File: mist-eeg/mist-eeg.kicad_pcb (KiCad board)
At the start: 4 copper layers, 50 x 75 mm, 234 parts, among them J1 Power_5V-14V, J10 J1310, J3 Audio, J4 Electrodes, J5 Micro_SD_Card_Det, J6 Extra GPIOs, J7 Digital buses, J8 J1312, J9 J1311, Q1 NMOS_DGS (3V3), Q3 NMOS_DGS (3.3V), Q4 PMOS_DGS (3.3V @ 1A), SW1 START, SW2 USER, SW3 SD_RST, SW4 RESET, SW5 ONOFF, U1 LTC2947, U10 ADAU1372, U11 ADS1299, U12 NX5427001Z, U5 TPS63070, U6 LT3042xMSE, U7 LT3042xMSE, U8 TPS63070, U9 TPS63070

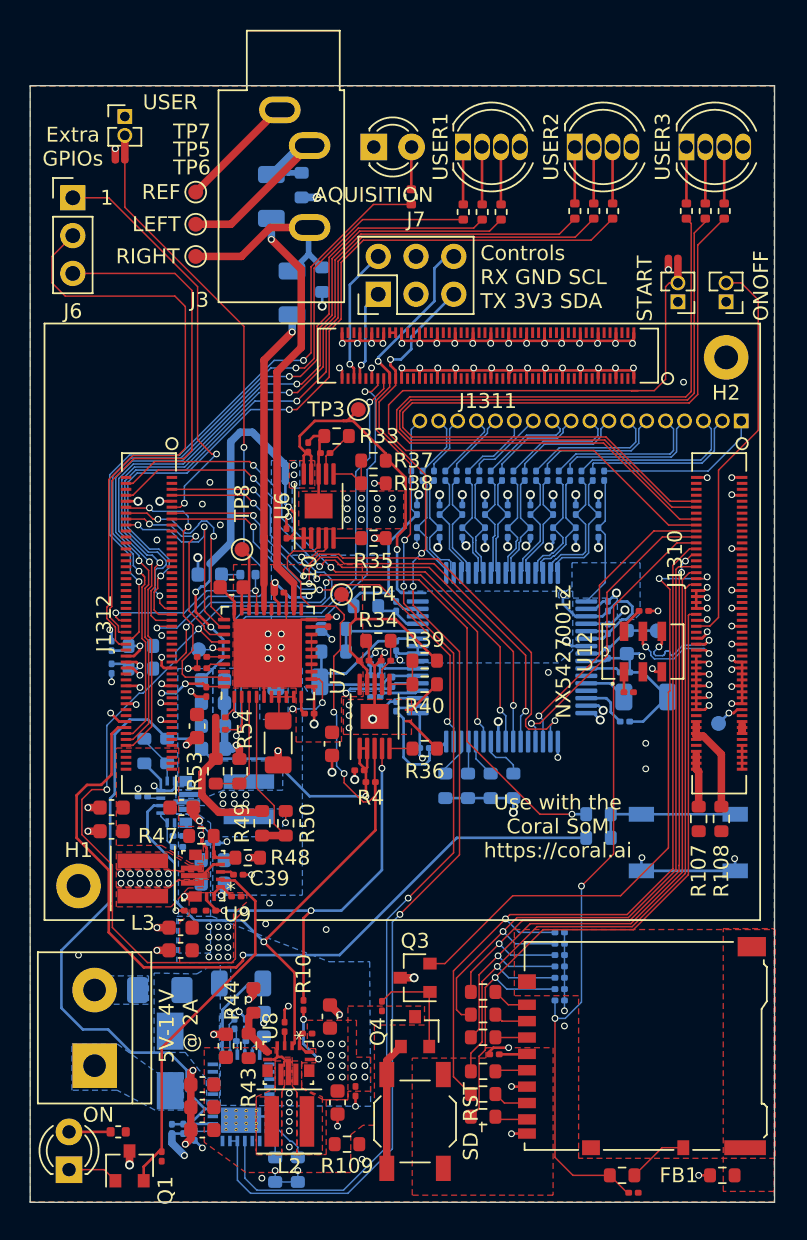
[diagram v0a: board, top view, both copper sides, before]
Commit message: Update footprints based upon piece availability & generate manufacturing files
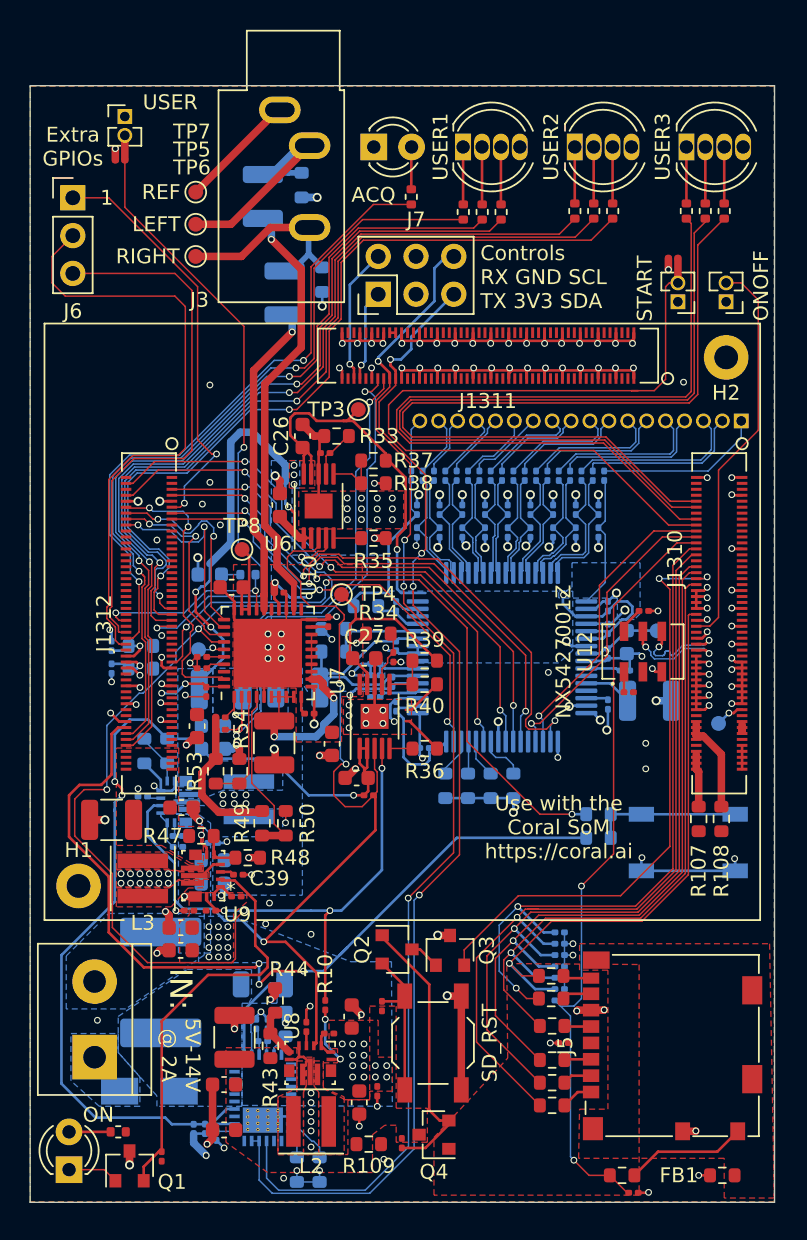
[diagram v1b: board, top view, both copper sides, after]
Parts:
- removed C21, C35, C42: 22uF, Capacitor_SMD:C_0603_1608Metric
- added Q2: NMOS_DGS (3.3V), Package_TO_SOT_SMD:SOT-23, F.Cu at (223.6, 92.0)
- added R11: 4k7, Resistor_SMD:R_0201_0603Metric, F.Cu at (222.6, 95.8)
- C19: value 22uF -> 10uF
- C20, C34, C41: value 22uF -> 47uF; footprint Capacitor_SMD:C_0603_1608Metric -> Capacitor_SMD:C_1210_3225Metric
- C22, C23, C26, C27: value 4u7F -> 10uF; footprint Capacitor_SMD:C_0201_0603Metric -> Capacitor_SMD:C_0603_1608Metric
- C44, C45, C50, C58, C65: footprint Capacitor_SMD:C_1206_3216Metric -> Capacitor_SMD:C_1210_3225Metric
- D5: value AQUISITION -> ACQ
- F1: footprint Fuse:Fuse_1206_3216Metric_Pad1.42x1.75mm_HandSolder -> Fuse:Fuse_2920_7451Metric
- J5: footprint Connector_Card:microSD_HC_Hirose_DM3AT-SF-PEJM5 -> Connector_Card:microSD_HC_Molex_104031-0811
- R47: value 52k5 -> 52k3
- moved R104 10.5 mm to (234.0, 93.8)
- moved R106 9.30 mm to (224.0, 105.0), turned to 270 degrees
- moved R99 8.92 mm to (234.1, 102.5)
- moved R103 7.88 mm to (234.0, 95.3)
- moved Q4 7.04 mm to (226.1, 104.5), turned to 180 degrees
- moved R100 6.51 mm to (234.1, 101.0)
- moved R102 5.55 mm to (234.1, 97.2)
- moved SW3 5.41 mm to (226.1, 98.3), turned to 270 degrees
- moved R101 4.88 mm to (234.1, 99.4)
- moved C87 4.70 mm to (234.8, 98.3)
- moved Q3 2.99 mm to (227.2, 92.1), turned to 90 degrees
- moved D1 2.47 mm to (207.0, 101.5), turned to 180 degrees
- moved J5 2.03 mm to (242.1, 98.5)
- moved C22 1.96 mm to (215.8, 62.2)
- moved C64 1.62 mm to (237.8, 75.6), turned to 90 degrees
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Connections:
- Q3 pad 1: Net-(Q3-Pad1) -> Net-(Q2-Pad3)
- Q4 pad 1: Net-(Q4-Pad1) -> /SD_DATA/+PWR
- Q4 pad 2: Net-(Q3-Pad1) -> Net-(Q2-Pad1)
- R106 pad 2: Net-(Q3-Pad1) -> Net-(Q2-Pad1)
- SW3 pad 1: Net-(Q4-Pad1) -> GND
- SW3 pad 2: /SD_DATA/+PWR -> Net-(Q2-Pad2)
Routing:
- net Net-(Q2-Pad1): track 0.00 -> 18.7 mm
- net Net-(Q2-Pad2): track 0.00 -> 10.8 mm
- net /SD_CLK: track 48.2 -> 38.6 mm
- net /SD_DAT0: track 44.1 -> 53.4 mm, vias 3 -> 1
- net Net-(Q4-Pad1): track 8.58 -> 0.00 mm
- net Net-(Q3-Pad1): track 7.18 -> 0.00 mm
- net /SD_CMD: track 52.4 -> 45.4 mm, vias 1 -> 2
- net Net-(J5-Pad10): track 4.05 -> 8.17 mm
- net /audio/CM: track 11.8 -> 15.4 mm
- net /SD_DAT3: track 47.2 -> 43.7 mm
- net /SD_DAT1: track 46.4 -> 49.9 mm
- net /SoM/~PWR_ON~: track 53.8 -> 56.9 mm, vias 1 -> 3
- net /+5V0_ANA: track 53.9 -> 56.8 mm
- net /power/+5V25: track 93.6 -> 96.4 mm, vias 4 -> 6
- net /power/PG: track 25.0 -> 27.7 mm
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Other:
- board text added: "IN:"

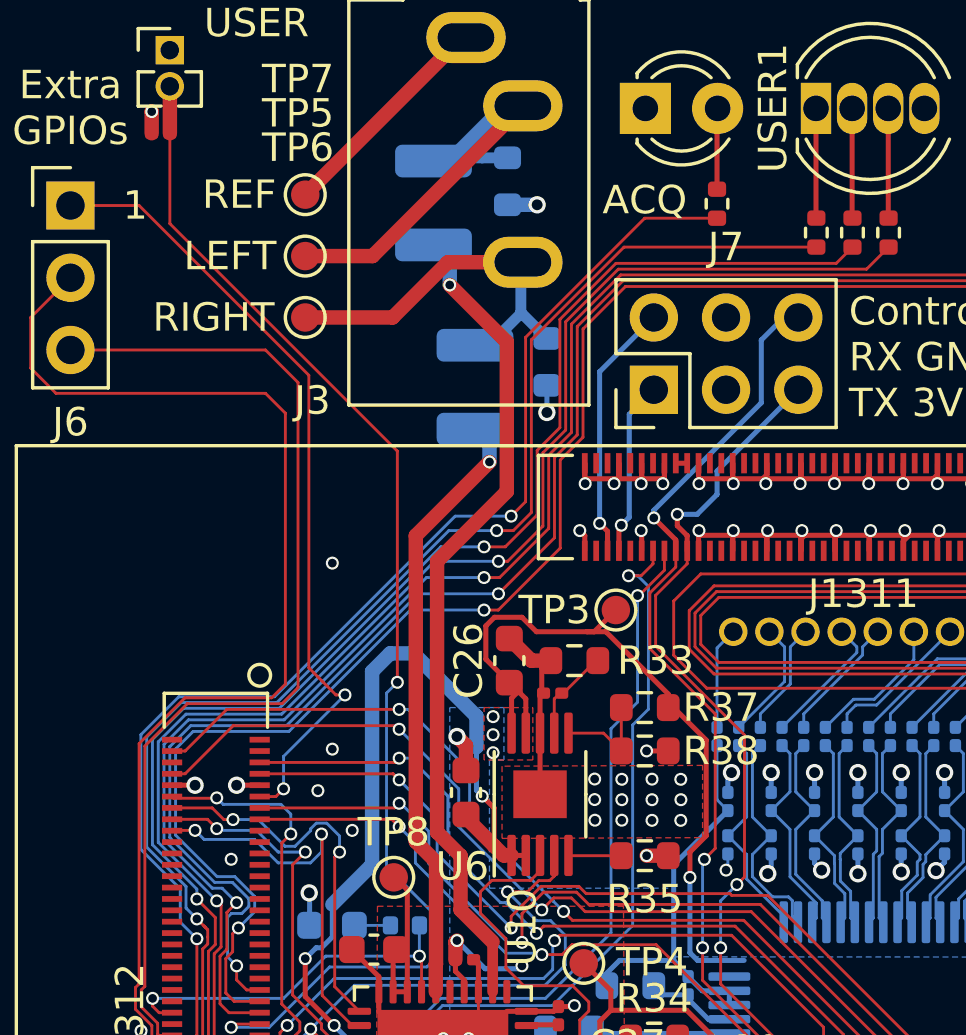
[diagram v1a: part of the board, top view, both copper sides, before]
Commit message: Small fix to the TPS63070 footprint
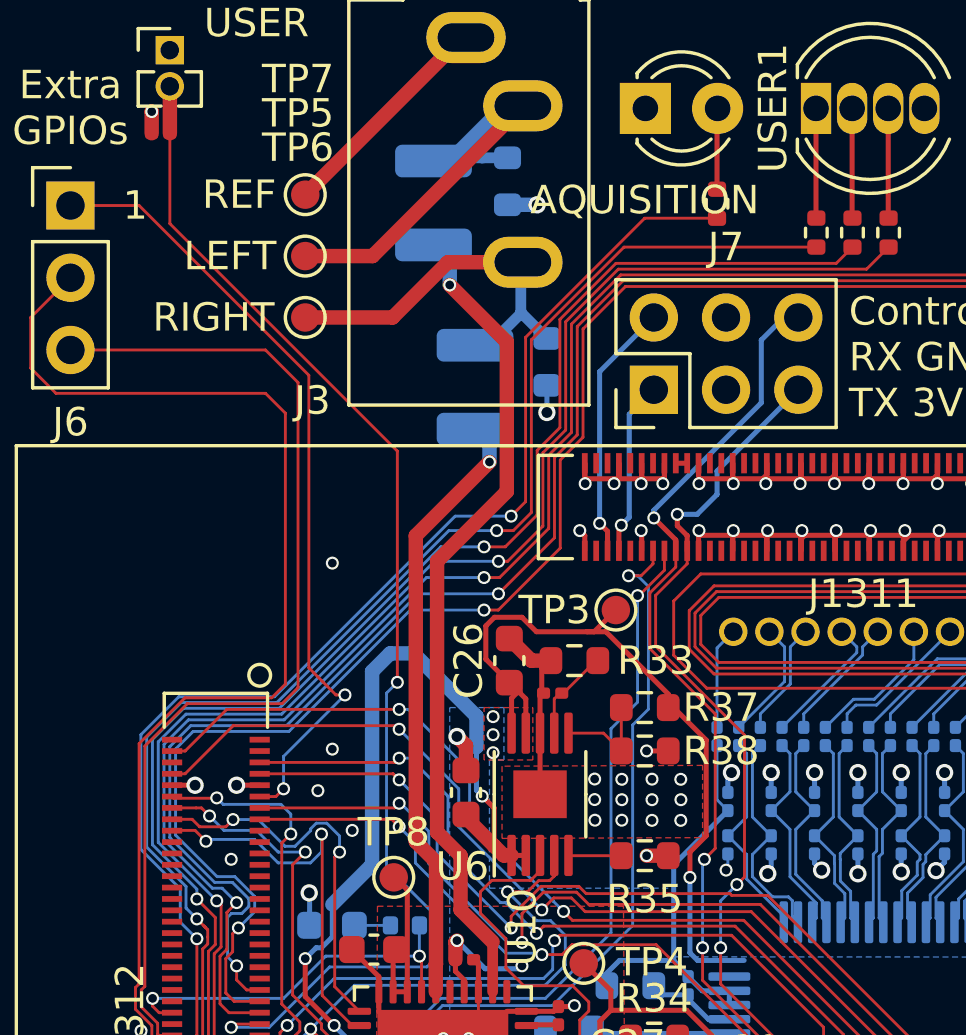
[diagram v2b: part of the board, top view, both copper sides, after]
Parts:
- D5: value ACQ -> AQUISITION
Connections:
- J8 pad 14: /AUDIO_LRCLK -> /AUDIO_SDATA
- J8 pad 16: /AUDIO_SDATA -> /AUDIO_LRCLK
